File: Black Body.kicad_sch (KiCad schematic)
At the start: 36 parts, among them IC2 MCP96L00T-E_MX, J1 53307-2471, J3 Conn_01x04, J4 MX150_02x08_RightAngle

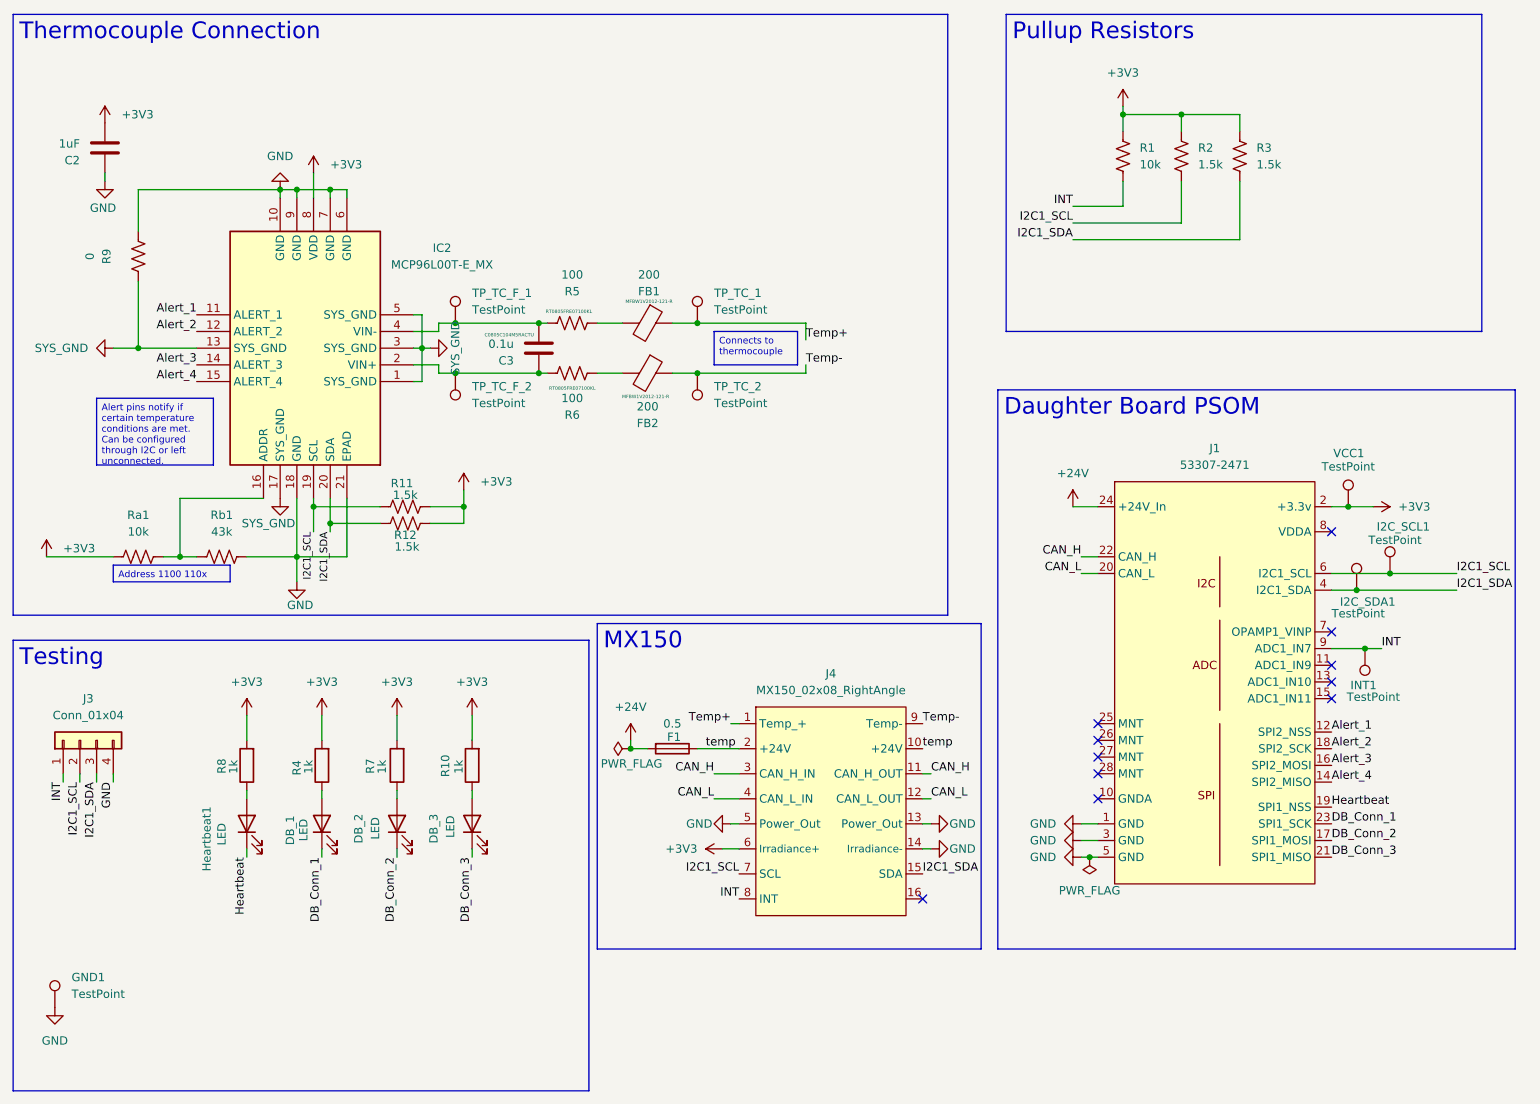
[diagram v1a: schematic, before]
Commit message: swap from mx150 to nanofit
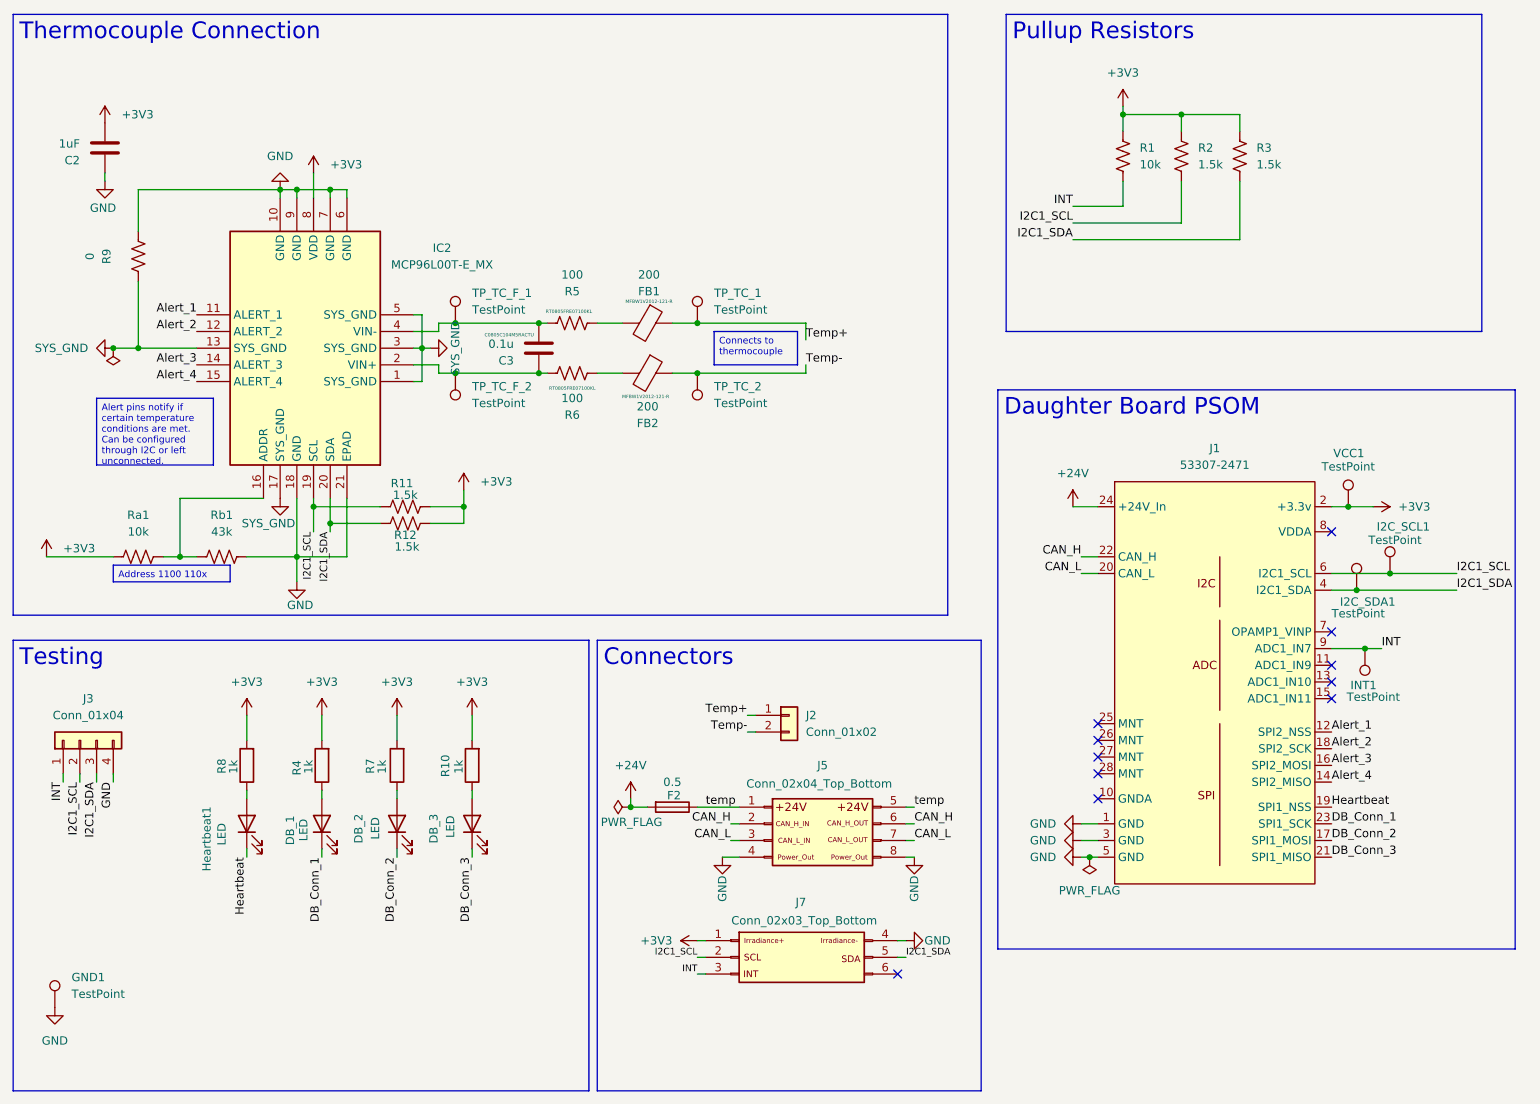
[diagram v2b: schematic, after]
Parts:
- removed F1: 0.5, Fuse:Fuseholder_Blade_Mini_Keystone_3568, symbol Device:Fuse
- removed J4: MX150_02x08_RightAngle, UTSVT-Conn:CONN_SD-75900-001_2X08_MOL, symbol utsvt_connectors:MX150_02x08_RightAngle
- added F2: 0.5, Fuse:Fuseholder_Blade_Mini_Keystone_3568, symbol Device:Fuse
- added J2: Conn_01x02, Connector_Molex:Molex_Nano-Fit_105313-xx02_1x02_P2.50mm_Horizontal, symbol Connector_Generic:Conn_01x02
- added J5: Conn_02x04_Top_Bottom, Connector_Molex:Molex_Nano-Fit_105314-xx08_2x04_P2.50mm_Horizontal, symbol Connector_Generic:Conn_02x04_Counter_Clockwise
- added J7: Conn_02x03_Top_Bottom, Connector_Molex:Molex_Nano-Fit_105314-xx06_2x03_P2.50mm_Horizontal, symbol Connector_Generic:Conn_02x03_Top_Bottom
- J3: footprint Connector_PinHeader_2.54mm:PinHeader_1x04_P2.54mm_Horizontal -> Connector_Molex:Molex_Nano-Fit_105313-xx04_1x04_P2.50mm_Horizontal
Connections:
- net +24V: now also F2.2
- net +3V3: now also J7.1 (Pin_1)
- net CAN_H: now also J5.2 (Pin_2), J5.6 (Pin_6)
- net CAN_L: now also J5.3 (Pin_3), J5.7 (Pin_7)
- net GND: now also J5.4 (Pin_4), J5.8 (Pin_8), J7.4 (Pin_4)
- net I2C1_SCL: now also J7.2 (Pin_2)
- net I2C1_SDA: now also J7.5 (Pin_5)
- net INT: now also J7.3 (Pin_3)
- net Temp+: now also J2.1 (Pin_1)
- net Temp-: now also J2.2 (Pin_2)
- net temp: now also F2.1, J5.1 (Pin_1), J5.5 (Pin_5)
